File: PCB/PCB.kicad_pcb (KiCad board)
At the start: 2 copper layers, 97.1 x 54 mm, 11 parts, among them J1 Conn_01x08_Pin, SW1 SW_Push, SW2 SW_Push, SW3 SW_Push, SW4 SW_Push, U1 XIAO-ESP32-C3-SMD

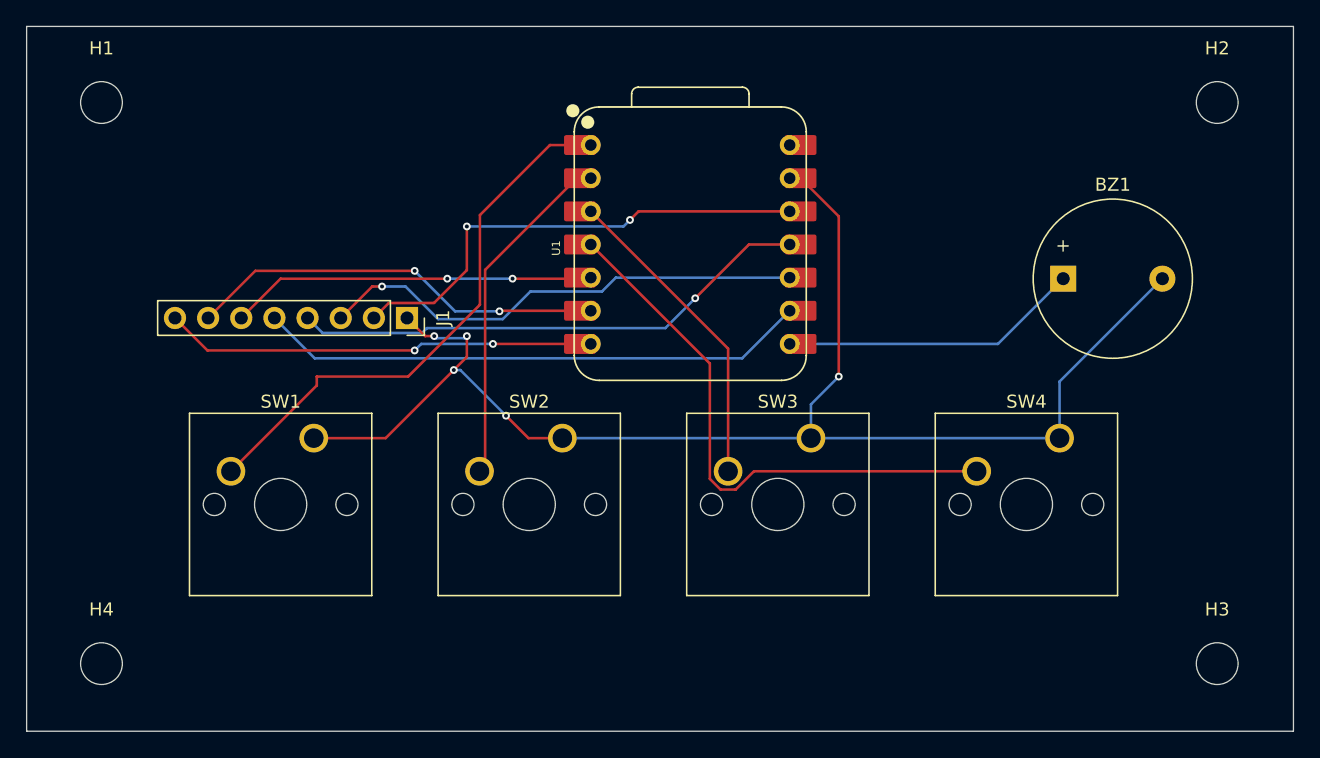
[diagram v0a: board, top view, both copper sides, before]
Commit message: Added svgs to the pcb
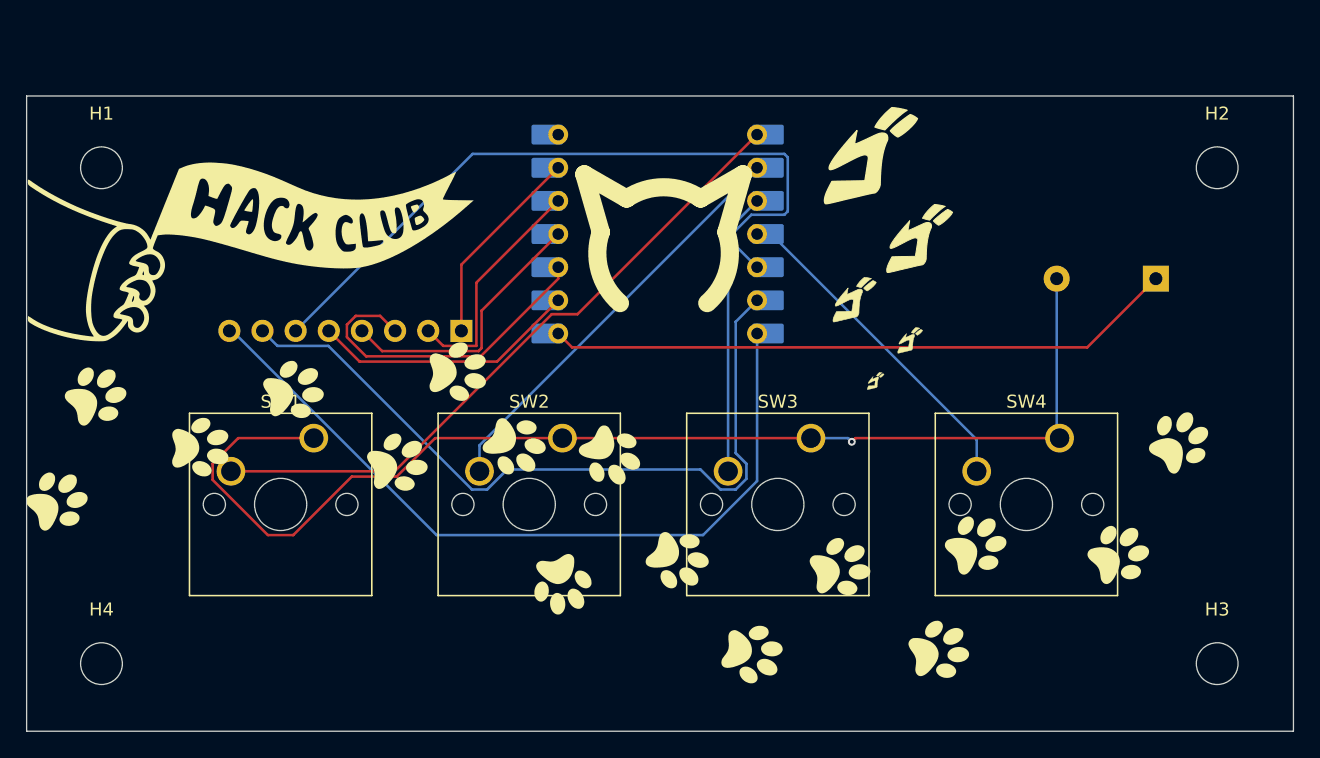
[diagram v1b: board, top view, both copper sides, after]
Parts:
- BZ1, J1, U1: moved to B.Cu
- moved BZ1 7.10 mm to (129.3, 97.0), turned to 180 degrees
- moved H1 5.00 mm to (48.5, 88.5)
- moved H2 5.00 mm to (134.0, 88.5)
- moved J1 4.28 mm to (76.1, 101.0), turned to 90 degrees
- moved U1 2.62 mm to (91.1, 93.6)
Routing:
- net /DC: track 28.1 -> 55.8 mm, vias 2 -> 0
- net /BL: track 33.1 -> 59.9 mm, vias 2 -> 0
- net /CS: track 32.1 -> 58.4 mm, vias 2 -> 0
- net Net-(BZ1-+): track 23.0 -> 48.4 mm
- net /RST: track 42.3 -> 20.5 mm
- net /+3.3V: track 37.2 -> 17.9 mm, vias 2 -> 0
- net /SDA: track 40.2 -> 21.1 mm, vias 1 -> 0
- net Net-(U1-D3): track 43.1 -> 25.8 mm
- net /SCL: track 37.8 -> 25.5 mm, vias 1 -> 0
- net Net-(U1-D0): track 42.4 -> 51.0 mm
- net Net-(U1-D1): track 26.6 -> 32.1 mm
- net Net-(U1-D2): track 24.3 -> 21.6 mm
- net /GND: track 107.3 -> 107.6 mm, vias 5 -> 1
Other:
- board size 97.1 x 54 mm -> 97.1 x 48.7 mm

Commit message: Adding more svgs to pcb
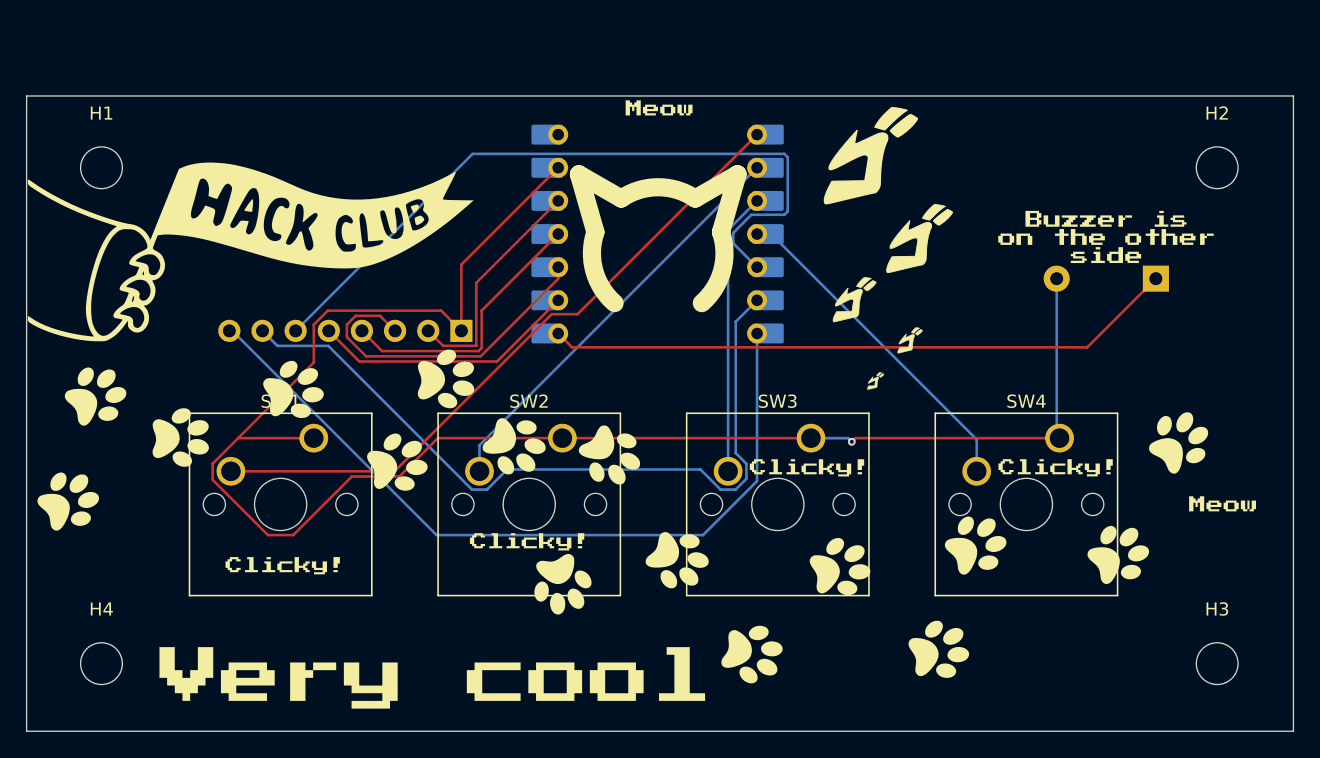
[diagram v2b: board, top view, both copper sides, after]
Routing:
- net /GND: track 107.6 -> 131.1 mm
